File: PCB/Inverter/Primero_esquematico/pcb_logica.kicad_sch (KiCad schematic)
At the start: 0 parts

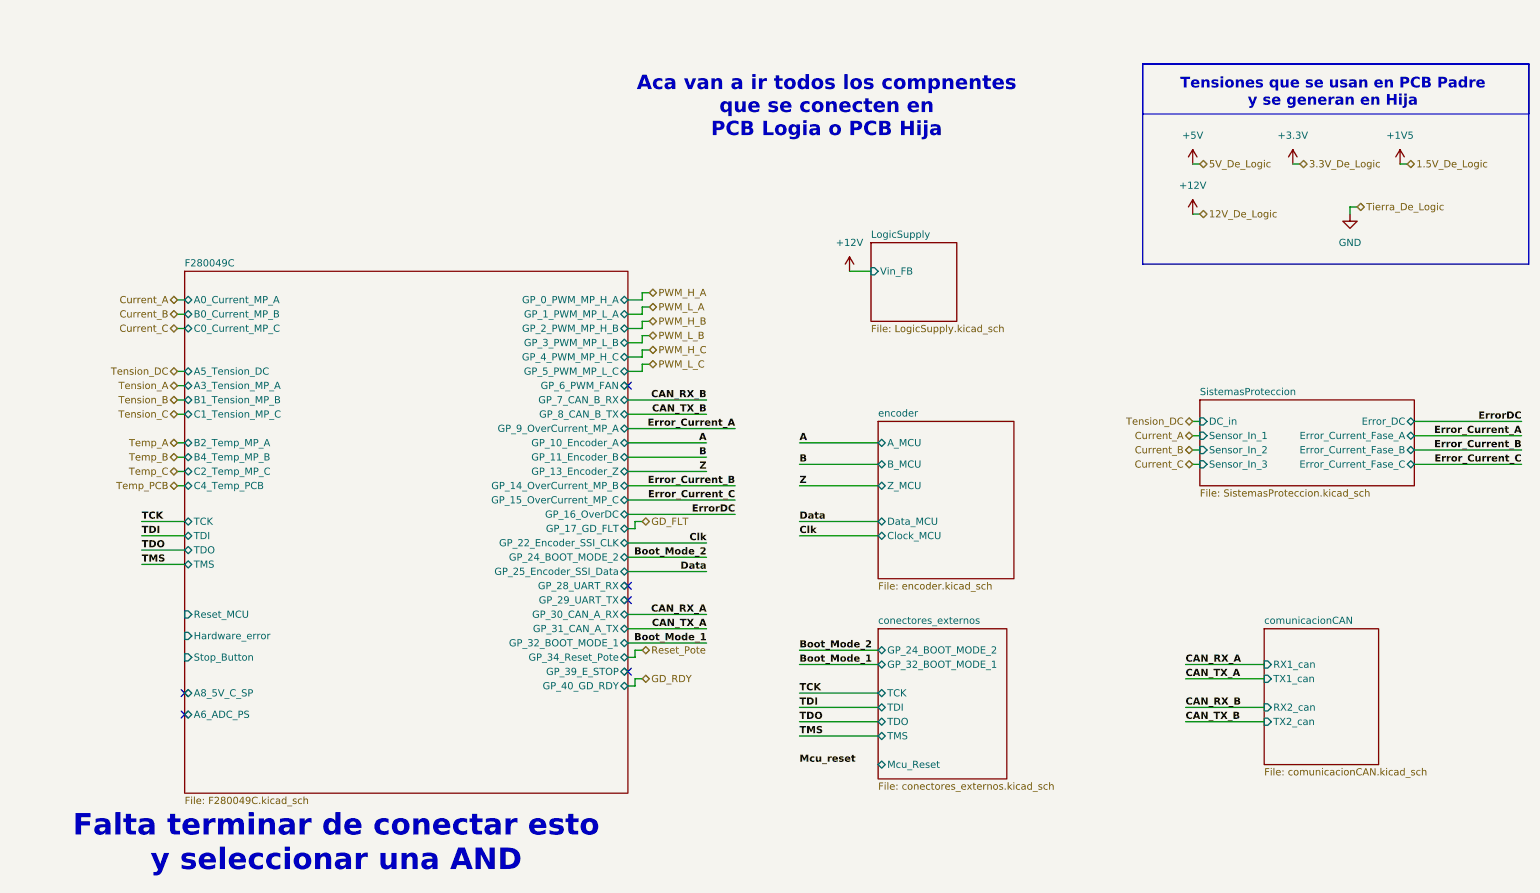
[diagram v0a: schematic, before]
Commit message: Un par de cosas q corregi del ERC pero sigue mal
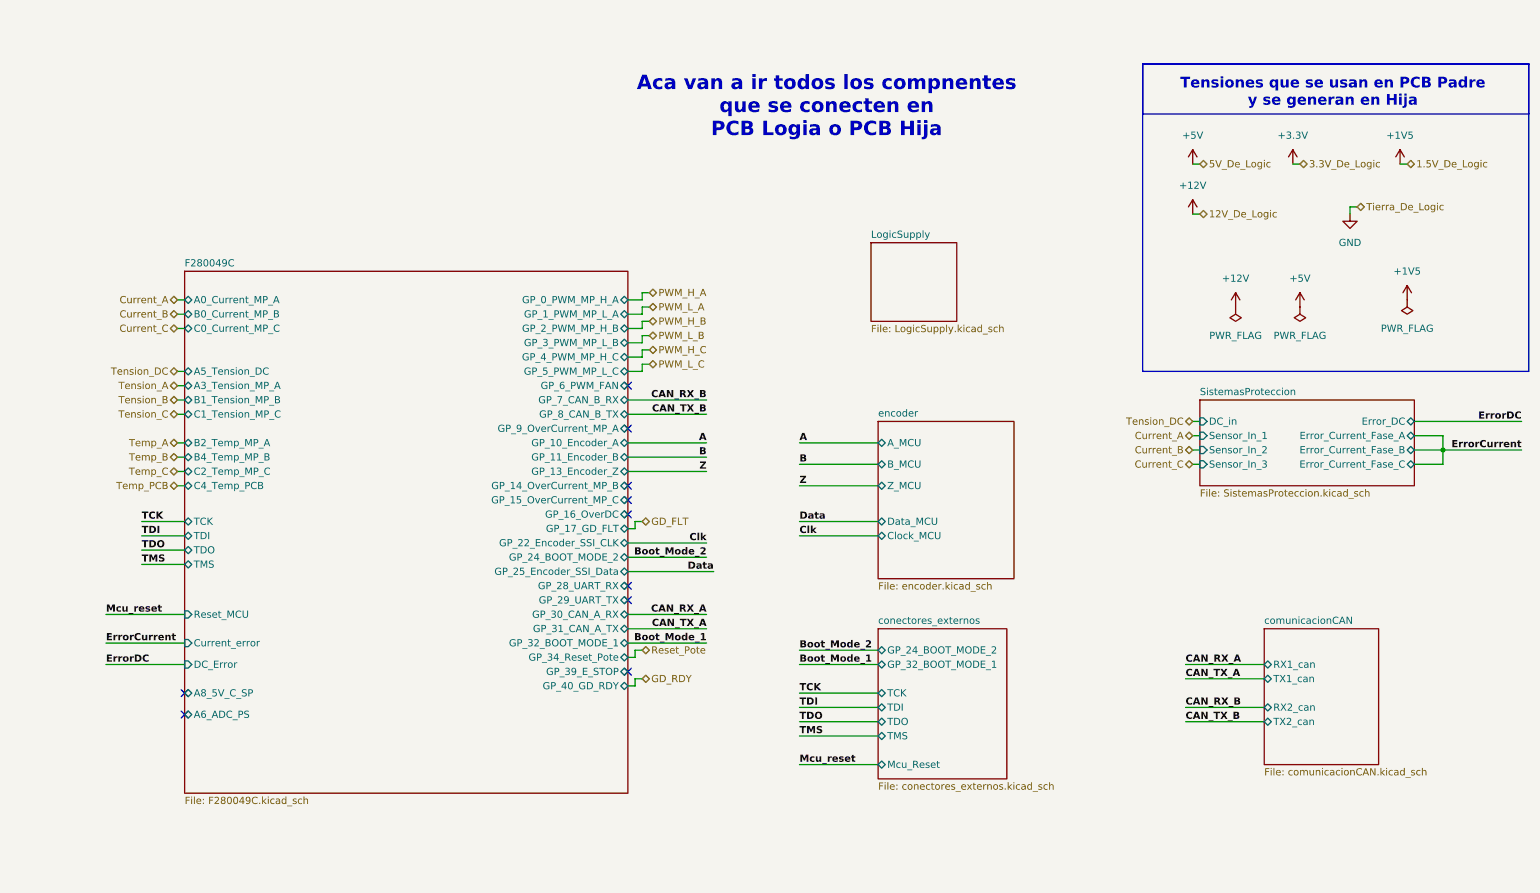
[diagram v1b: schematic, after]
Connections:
- no-connect marks 6 -> 10
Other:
- sheet F280049C ports: added Current_error, DC_Error; removed Hardware_error, Stop_Button
- sheet LogicSupply ports: added none; removed Vin_FB
- note removed: "Falta terminar de conectar esto y seleccionar una AND"

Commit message: Esquematico Listo
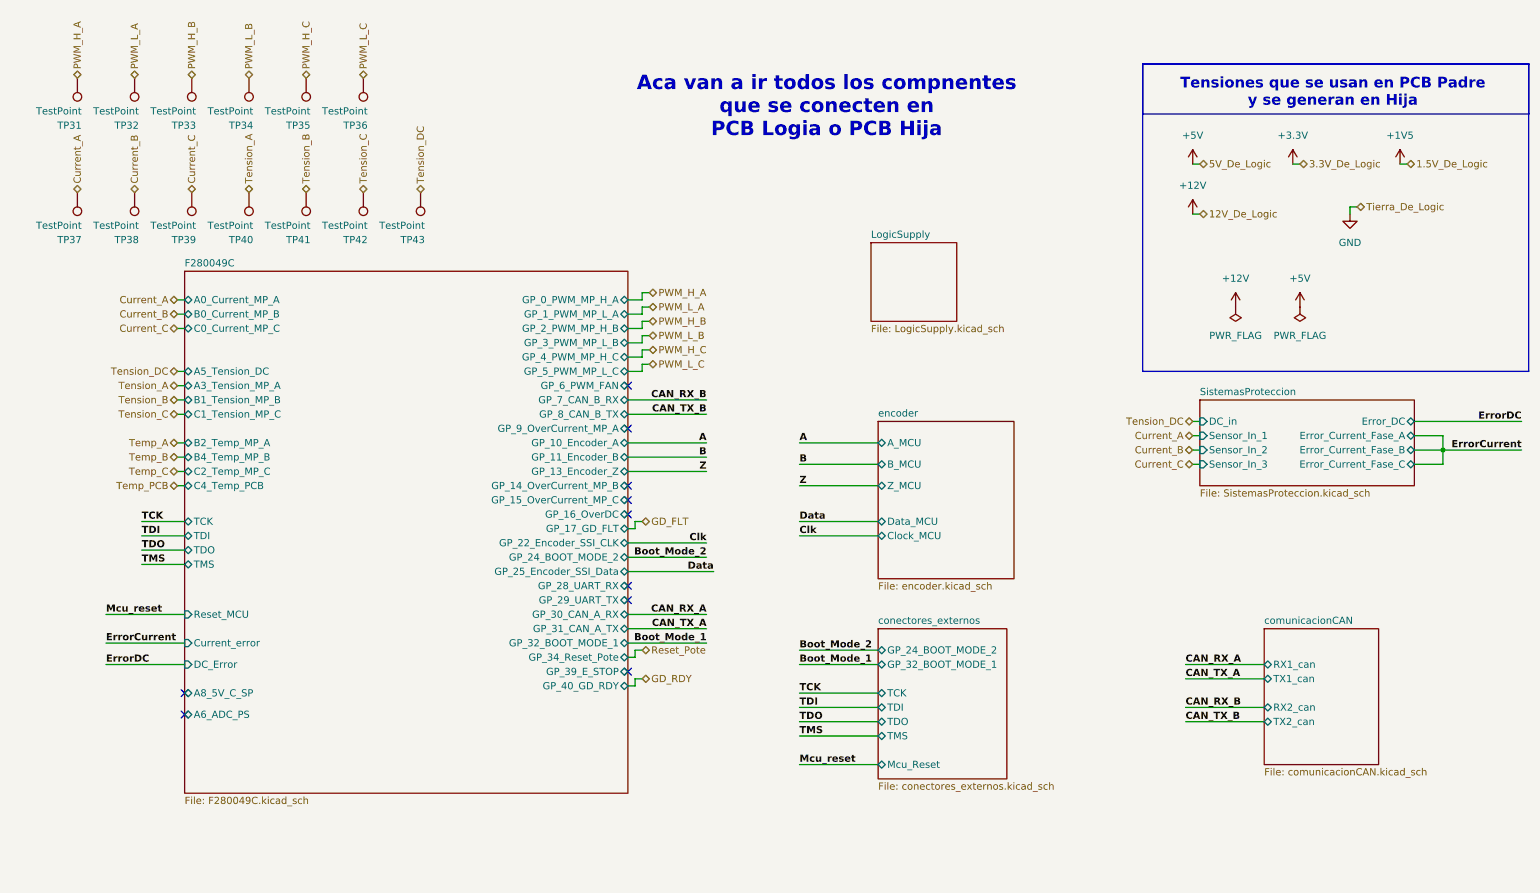
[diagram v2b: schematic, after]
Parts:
- added TP31, TP32, TP33, TP34, TP35, TP36, TP37, TP38, TP39, TP40, TP41, TP42, TP43: TestPoint, TestPoint:TestPoint_Pad_D2.0mm, symbol Connector:TestPoint
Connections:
- net Current_A: now also TP37.1
- net Current_B: now also TP38.1
- net Current_C: now also TP39.1
- net PWM_H_A: now also TP31.1
- net PWM_H_B: now also TP33.1
- net PWM_H_C: now also TP35.1
- net PWM_L_A: now also TP32.1
- net PWM_L_B: now also TP34.1
- net PWM_L_C: now also TP36.1
- net Tension_A: now also TP40.1
- net Tension_B: now also TP41.1
- net Tension_C: now also TP42.1
- net Tension_DC: now also TP43.1

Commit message: correcciones
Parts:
- TP52: renamed from TP31; footprint TestPoint:TestPoint_Pad_D2.0mm -> TestPoint:TestPoint_Pad_D1.0mm
- TP53: renamed from TP37; footprint TestPoint:TestPoint_Pad_D2.0mm -> TestPoint:TestPoint_Pad_D1.0mm
- TP54: renamed from TP32; footprint TestPoint:TestPoint_Pad_D2.0mm -> TestPoint:TestPoint_Pad_D1.0mm
- TP55: renamed from TP38; footprint TestPoint:TestPoint_Pad_D2.0mm -> TestPoint:TestPoint_Pad_D1.0mm
- TP56: renamed from TP33; footprint TestPoint:TestPoint_Pad_D2.0mm -> TestPoint:TestPoint_Pad_D1.0mm
- TP57: renamed from TP39; footprint TestPoint:TestPoint_Pad_D2.0mm -> TestPoint:TestPoint_Pad_D1.0mm
- TP58: renamed from TP34; footprint TestPoint:TestPoint_Pad_D2.0mm -> TestPoint:TestPoint_Pad_D1.0mm
- TP59: renamed from TP40; footprint TestPoint:TestPoint_Pad_D2.0mm -> TestPoint:TestPoint_Pad_D1.0mm
- TP60: renamed from TP35; footprint TestPoint:TestPoint_Pad_D2.0mm -> TestPoint:TestPoint_Pad_D1.0mm
- TP61: renamed from TP41; footprint TestPoint:TestPoint_Pad_D2.0mm -> TestPoint:TestPoint_Pad_D1.0mm
- TP62: renamed from TP36; footprint TestPoint:TestPoint_Pad_D2.0mm -> TestPoint:TestPoint_Pad_D1.0mm
- TP63: renamed from TP42; footprint TestPoint:TestPoint_Pad_D2.0mm -> TestPoint:TestPoint_Pad_D1.0mm
- TP64: renamed from TP43; footprint TestPoint:TestPoint_Pad_D2.0mm -> TestPoint:TestPoint_Pad_D1.0mm

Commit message: Corregi cosas de la placa
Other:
- note removed: "Tensiones que se usan en PCB Padre y se generan en Hija"

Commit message: Modificaciones varias
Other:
- sheet F280049C ports: added GP_12_CAN_B_TX, GP_13_CAN_B_RX, GP_14_OverCurrent_MP_A, GP_15_OverCurrent_MP_B, GP_16_OverCurrent_MP_C, GP_17_OverDC, GP_22_GD_FLT, GP_7_Encoder_SSI_Data, GP_8_Encoder_SSI_CLK, GP_9_Encoder_Z; removed GP_13_Encoder_Z, GP_14_OverCurrent_MP_B, GP_15_OverCurrent_MP_C, GP_16_OverDC, GP_17_GD_FLT, GP_22_Encoder_SSI_CLK, GP_25_Encoder_SSI_Data, GP_7_CAN_B_RX, GP_8_CAN_B_TX, GP_9_OverCurrent_MP_A
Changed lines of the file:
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@@
 	)
 	(no_connect
-		(at 119.38 96.52)
+		(at 119.38 144.78)
 	)
 	(no_connect
@@
 	)
 	(no_connect
-		(at 119.38 101.6)
+		(at 119.38 78.74)
 	)
 	(no_connect
-		(at 119.38 99.06)
+		(at 119.38 147.32)
 	)
 	(no_connect
-		(at 119.38 78.74)
+		(at 119.38 142.24)
 	)
 	(no_connect
-		(at 119.38 86.36)
+		(at 40.64 137.16)
 	)
 	(no_connect
-		(at 40.64 137.16)
+		(at 119.38 139.7)
 	)
 	(wire
@@
 	(wire
 		(pts
+			(xy 133.35 99.06) (xy 119.38 99.06)
+		)
+		(stroke
+			(width 0)
+			(type default)
+		)
+	)
+	(wire
+		(pts
 			(xy 39.37 81.28) (xy 40.64 81.28)
 		)
@@
 	(wire
 		(pts
+			(xy 133.35 96.52) (xy 119.38 96.52)
+		)
+		(stroke
+			(width 0)
+			(type default)
+		)
+	)
+	(wire
+		(pts
 			(xy 26.67 119.38) (xy 40.64 119.38)
 		)
@@
 	(wire
 		(pts
-			(xy 120.65 127) (xy 119.38 127)
+			(xy 119.38 91.44) (xy 133.35 91.44)
 		)
 		(stroke
@@
 	(wire
 		(pts
-			(xy 119.38 132.08) (xy 120.65 132.08)
+			(xy 120.65 127) (xy 119.38 127)
 		)
 		(stroke
@@
 	(wire
 		(pts
-			(xy 133.35 88.9) (xy 119.38 88.9)
+			(xy 119.38 132.08) (xy 120.65 132.08)
 		)
 		(stroke
@@
 	(wire
 		(pts
-			(xy 133.35 91.44) (xy 119.38 91.44)
+			(xy 119.38 88.9) (xy 133.35 88.9)
 		)
 		(stroke
@@
 	(wire
 		(pts
-			(xy 134.62 111.76) (xy 119.38 111.76)
-		)
-		(stroke
-			(width 0)
-			(type default)
-		)
-	)
-	(wire
-		(pts
 			(xy 120.65 132.08) (xy 120.65 130.81)
 		)
@@
 	(wire
 		(pts
-			(xy 133.35 106.68) (xy 119.38 106.68)
-		)
-		(stroke
-			(width 0)
-			(type default)
-		)
-	)
-	(wire
-		(pts
 			(xy 120.65 130.81) (xy 121.92 130.81)
 		)
@@
 		)
 	)
+	(label "Data"
+		(at 133.35 96.52 180)
+		(effects
+			(font
+				(size 1.27 1.27)
+				(thickness 0.254)
+				(bold yes)
+			)
+			(justify right bottom)
+		)
+	)
 	(label "TCK"
 		(at 33.02 102.87 0)
@@
 		)
 	)
+	(label "Clk"
+		(at 133.35 99.06 180)
+		(effects
+			(font
+				(size 1.27 1.27)
+				(thickness 0.254)
+				(bold yes)
+			)
+			(justify right bottom)
+		)
+	)
 	(label "B"
 		(at 133.35 91.44 180)
@@
 	)
 	(label "Data"
-		(at 134.62 111.76 180)
-		(effects
-			(font
-				(size 1.27 1.27)
-				(thickness 0.254)
-				(bold yes)
-			)
-			(justify right bottom)
-		)
-	)
-	(label "Data"
 		(at 149.86 102.87 0)
 		(effects
@@
 		)
 	)
-	(label "Clk"
-		(at 133.35 106.68 180)
-		(effects
-			(font
-				(size 1.27 1.27)
-				(thickness 0.254)
-				(bold yes)
-			)
-			(justify right bottom)
-		)
-	)
 	(label "TCK"
 		(at 149.86 133.35 0)
@@
 			)
 		)
-		(pin "GP_7_CAN_B_RX" bidirectional
-			(at 119.38 81.28 0)
+		(pin "GP_24_BOOT_MODE_2" bidirectional
+			(at 119.38 109.22 0)
 			(effects
 				(font
@@
 			)
 		)
-		(pin "GP_8_CAN_B_TX" bidirectional
-			(at 119.38 83.82 0)
+		(pin "GP_28_UART_RX" bidirectional
+			(at 119.38 114.3 0)
 			(effects
 				(font
@@
 			)
 		)
-		(pin "GP_9_OverCurrent_MP_A" bidirectional
-			(at 119.38 86.36 0)
+		(pin "GP_29_UART_TX" bidirectional
+			(at 119.38 116.84 0)
 			(effects
 				(font
@@
 			)
 		)
-		(pin "GP_10_Encoder_A" bidirectional
-			(at 119.38 88.9 0)
+		(pin "GP_30_CAN_A_RX" bidirectional
+			(at 119.38 119.38 0)
 			(effects
 				(font
@@
 			)
 		)
-		(pin "GP_11_Encoder_B" bidirectional
-			(at 119.38 91.44 0)
+		(pin "GP_31_CAN_A_TX" bidirectional
+			(at 119.38 121.92 0)
 			(effects
 				(font
@@
 			)
 		)
-		(pin "GP_13_Encoder_Z" bidirectional
-			(at 119.38 93.98 0)
+		(pin "GP_32_BOOT_MODE_1" bidirectional
+			(at 119.38 124.46 0)
 			(effects
 				(font
@@
 			)
 		)
-		(pin "GP_14_OverCurrent_MP_B" bidirectional
-			(at 119.38 96.52 0)
+		(pin "GP_34_Reset_Pote" bidirectional
+			(at 119.38 127 0)
 			(effects
 				(font
@@
 			)
 		)
-		(pin "GP_15_OverCurrent_MP_C" bidirectional
-			(at 119.38 99.06 0)
+		(pin "GP_39_E_STOP" bidirectional
+			(at 119.38 129.54 0)
 			(effects
 				(font
@@
 			)
 		)
-		(pin "GP_16_OverDC" bidirectional
-			(at 119.38 101.6 0)
+		(pin "GP_40_GD_RDY" bidirectional
+			(at 119.38 132.08 0)
 			(effects
 				(font
@@
 			)
 		)
-		(pin "GP_17_GD_FLT" bidirectional
-			(at 119.38 104.14 0)
+		(pin "Reset_MCU" input
+			(at 40.64 119.38 180)
 			(effects
 				(font
 					(size 1.27 1.27)
 				)
-				(justify right)
+				(justify left)
 			)
 		)
-		(pin "GP_22_Encoder_SSI_CLK" bidirectional
-			(at 119.38 106.68 0)
+		(pin "TCK" bidirectional
+			(at 40.64 102.87 180)
 			(effects
 				(font
 					(size 1.27 1.27)
 				)
-				(justify right)
+				(justify left)
 			)
 		)
-		(pin "GP_24_BOOT_MODE_2" bidirectional
-			(at 119.38 109.22 0)
+		(pin "TDI" bidirectional
+			(at 40.64 105.41 180)
 			(effects
 				(font
 					(size 1.27 1.27)
 				)
-				(justify right)
+				(justify left)
 			)
 		)
-		(pin "GP_25_Encoder_SSI_Data" bidirectional
-			(at 119.38 111.76 0)
+		(pin "TDO" bidirectional
+			(at 40.64 107.95 180)
 			(effects
 				(font
 					(size 1.27 1.27)
 				)
-				(justify right)
+				(justify left)
 			)
 		)
-		(pin "GP_28_UART_RX" bidirectional
-			(at 119.38 114.3 0)
+		(pin "TMS" bidirectional
+			(at 40.64 110.49 180)
 			(effects
 				(font
 					(size 1.27 1.27)
 				)
-				(justify right)
+				(justify left)
 			)
 		)
-		(pin "GP_29_UART_TX" bidirectional
-			(at 119.38 116.84 0)
+		(pin "Current_error" input
+			(at 40.64 124.46 180)
 			(effects
 				(font
 					(size 1.27 1.27)
 				)
-				(justify right)
+				(justify left)
 			)
 		)
-		(pin "GP_30_CAN_A_RX" bidirectional
-			(at 119.38 119.38 0)
+		(pin "DC_Error" input
+			(at 40.64 128.27 180)
 			(effects
 				(font
 					(size 1.27 1.27)
 				)
-				(justify right)
+				(justify left)
 			)
 		)
-		(pin "GP_31_CAN_A_TX" bidirectional
-			(at 119.38 121.92 0)
+		(pin "GP_7_Encoder_SSI_Data" bidirectional
+			(at 119.38 96.52 0)
 			(effects
 				(font
@@
 			)
 		)
-		(pin "GP_32_BOOT_MODE_1" bidirectional
-			(at 119.38 124.46 0)
+		(pin "GP_8_Encoder_SSI_CLK" bidirectional
+			(at 119.38 99.06 0)
 			(effects
 				(font
@@
 			)
 		)
-		(pin "GP_34_Reset_Pote" bidirectional
-			(at 119.38 127 0)
+		(pin "GP_9_Encoder_Z" bidirectional
+			(at 119.38 93.98 0)
 			(effects
 				(font
@@
 			)
 		)
-		(pin "GP_39_E_STOP" bidirectional
-			(at 119.38 129.54 0)
+		(pin "GP_10_Encoder_A" bidirectional
+			(at 119.38 88.9 0)
 			(effects
 				(font
@@
 			)
 		)
-		(pin "GP_40_GD_RDY" bidirectional
-			(at 119.38 132.08 0)
+		(pin "GP_11_Encoder_B" bidirectional
+			(at 119.38 91.44 0)
 			(effects
 				(font
@@
 			)
 		)
-		(pin "Reset_MCU" input
-			(at 40.64 119.38 180)
+		(pin "GP_12_CAN_B_TX" bidirectional
+			(at 119.38 83.82 0)
 			(effects
 				(font
 					(size 1.27 1.27)
 				)
-				(justify left)
+				(justify right)
 			)
 		)
-		(pin "TCK" bidirectional
-			(at 40.64 102.87 180)
+		(pin "GP_13_CAN_B_RX" bidirectional
+			(at 119.38 81.28 0)
 			(effects
 				(font
 					(size 1.27 1.27)
 				)
-				(justify left)
+				(justify right)
 			)
 		)
-		(pin "TDI" bidirectional
-			(at 40.64 105.41 180)
+		(pin "GP_14_OverCurrent_MP_A" bidirectional
+			(at 119.38 139.7 0)
 			(effects
 				(font
 					(size 1.27 1.27)
 				)
-				(justify left)
+				(justify right)
 			)
 		)
-		(pin "TDO" bidirectional
-			(at 40.64 107.95 180)
+		(pin "GP_15_OverCurrent_MP_B" bidirectional
+			(at 119.38 142.24 0)
 			(effects
 				(font
 					(size 1.27 1.27)
 				)
-				(justify left)
+				(justify right)
 			)
 		)
-		(pin "TMS" bidirectional
-			(at 40.64 110.49 180)
+		(pin "GP_16_OverCurrent_MP_C" bidirectional
+			(at 119.38 144.78 0)
 			(effects
 				(font
 					(size 1.27 1.27)
 				)
-				(justify left)
+				(justify right)
 			)
 		)
-		(pin "Current_error" input
-			(at 40.64 124.46 180)
+		(pin "GP_17_OverDC" bidirectional
+			(at 119.38 147.32 0)
 			(effects
 				(font
 					(size 1.27 1.27)
 				)
-				(justify left)
+				(justify right)
 			)
 		)
-		(pin "DC_Error" input
-			(at 40.64 128.27 180)
+		(pin "GP_22_GD_FLT" bidirectional
+			(at 119.38 104.14 0)
 			(effects
 				(font
 					(size 1.27 1.27)
 				)
-				(justify left)
+				(justify right)
 			)
 		)
